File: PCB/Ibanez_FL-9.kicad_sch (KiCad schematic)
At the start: 131 parts, among them J1 INPUT, J2 OUTPUT, J3 EXT_DC, Q101 2SC2458GR, Q102 2SC2458GR, Q103 2SK44SPC, Q104 2SC2458GR, Q105 2SC2458GR, Q106 2SC2458GR, Q107 2SA1048Y/GR, Q108A 2SC1583F, Q108B 2SC1583F, Q109 2SC2458GR, U101 TL022, U102 TL022, U103 TL022, U104 MN3207, U105 MN3102, U106 LM2931-5.0_TO220

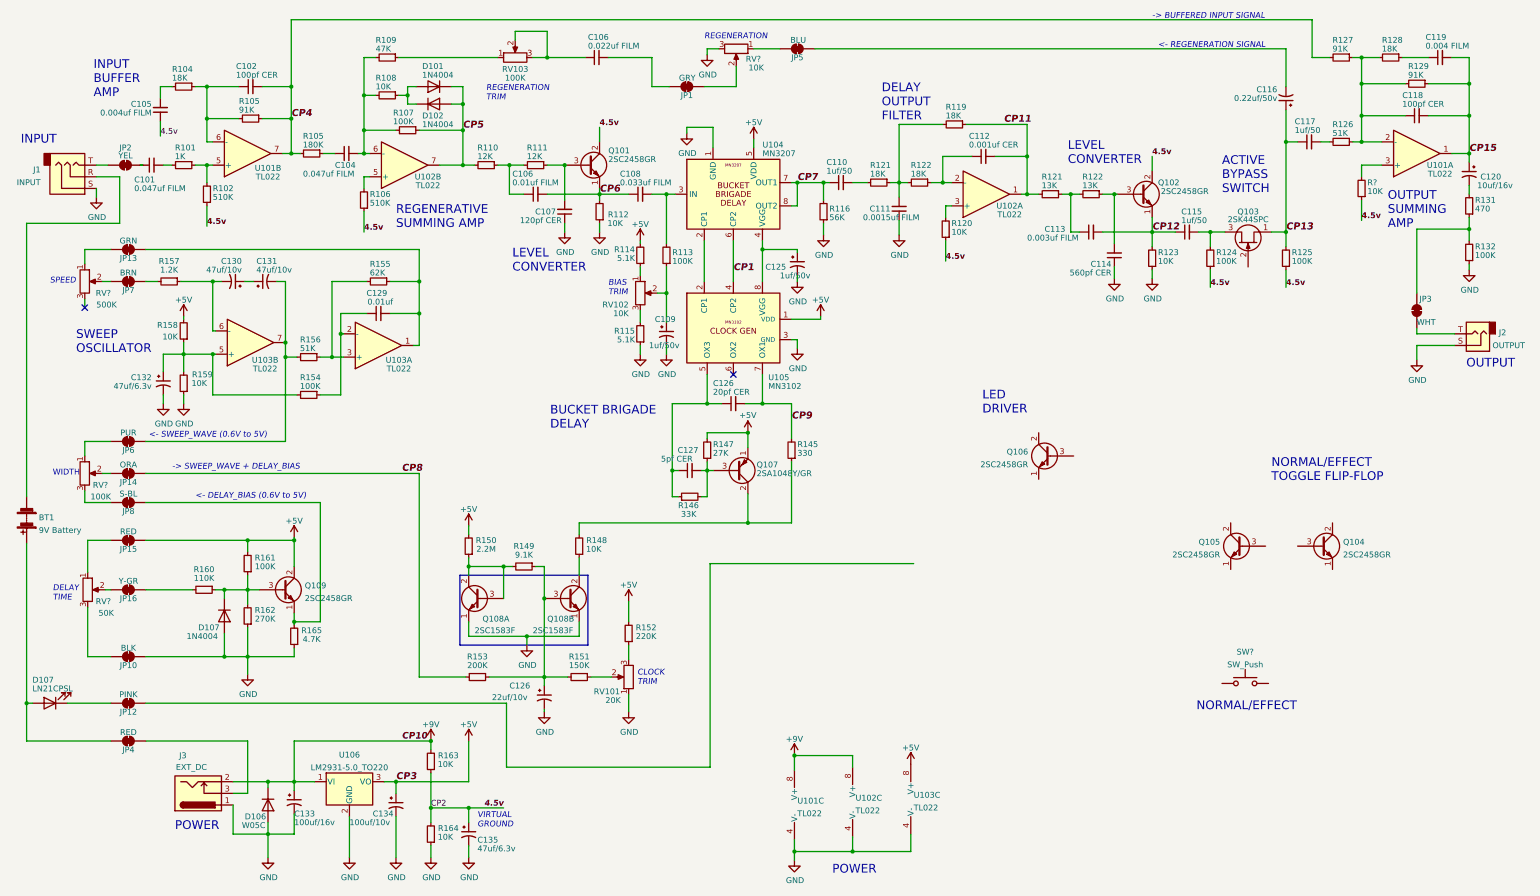
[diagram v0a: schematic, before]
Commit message: update docs; add BOM
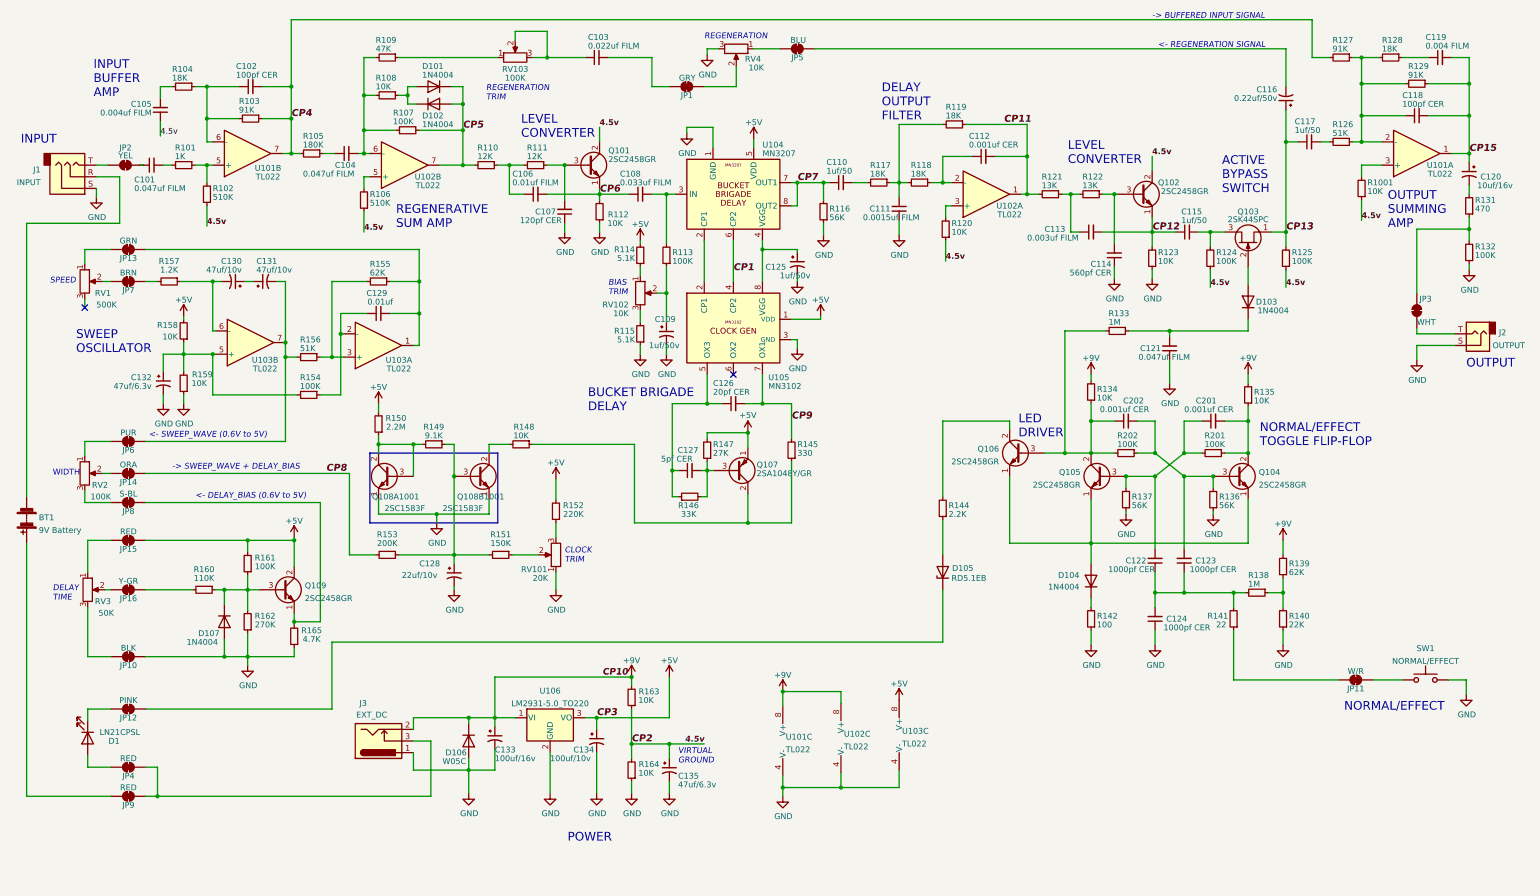
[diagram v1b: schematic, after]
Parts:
- added C121: 0.047uf FILM, Capacitor_SMD:C_0805_2012Metric, symbol Device:C_Small
- added C122, C123, C124: 1000pf CER, Capacitor_SMD:C_0805_2012Metric, symbol Device:C_Small
- added C201, C202: 0.001uf CER, Capacitor_SMD:C_0805_2012Metric, symbol Device:C_Small
- added D103, D104: 1N4004, Diode_THT:D_DO-35_SOD27_P7.62mm_Horizontal, symbol Diode:1N4448
- added D105: RD5.1EB, symbol Device:D_Zener
- added JP11: W/R, symbol Jumper:SolderJumper_2_Bridged
- added JP9: RED, symbol Jumper:SolderJumper_2_Bridged
- added R133, R138: 1M, Resistor_SMD:R_0805_2012Metric, symbol Device:R_Small
- added R134, R135: 10K, Resistor_SMD:R_0805_2012Metric, symbol Device:R_Small
- added R136, R137: 56K, Resistor_SMD:R_0805_2012Metric, symbol Device:R_Small
- added R139: 62K, Resistor_SMD:R_0805_2012Metric, symbol Device:R_Small
- added R140: 22K, Resistor_SMD:R_0805_2012Metric, symbol Device:R_Small
- added R141: 22, Resistor_SMD:R_0805_2012Metric, symbol Device:R_Small
- added R142: 100, Resistor_SMD:R_0805_2012Metric, symbol Device:R_Small
- added R144: 2.2K, Resistor_SMD:R_0805_2012Metric, symbol Device:R_Small
- added R201, R202: 100K, Resistor_SMD:R_0805_2012Metric, symbol Device:R_Small
- SW1: renamed from SW?; value SW_Push -> NORMAL/EFFECT
- gave numbers to parts that had none: 5
- renumbered C106 to C103, C126 to C128, D107 to D1, Q108A to Q108A1001, Q108B to Q108B1001, R105 to R103, R121 to R117, R122 to R118
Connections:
- net +9V: now also R134.2, R135.2, R139.2
- net GND: now also SW1.2, C121.1, C124.1, R136.1, R137.1, R140.1, R142.1
- net at D1.2 (A), JP4.1 (A): no longer BT1.1 (+)
- net at Q106.1 (E): now also Q104.1 (E), Q105.1 (E), D104.2 (A)
- net at Q106.2 (C): now also R144.2
- net at Q106.3 (B): now also Q105.2 (C), C202.1, R133.2, R134.1, R202.2
- net at Q108B1001.2 (C): now also R148.2; no longer R148.1
- net at JP12.2 (B): now also D105.1 (K)
- net at Q107.2 (C), R145.1: now also R148.1; no longer R148.2
- net at Q105.3 (B): now also C122.2, C201.1, R137.2, R201.2
- net at SW1.1: now also JP11.2 (B)
- net at Q104.2 (C): now also C201.2, R135.1, R201.1
- net at Q104.3 (B): now also C123.2, C202.2, R136.2, R202.1
- net at J3.3, JP4.2 (B): now also JP9.2 (B)
- net at Q103.2 (G): now also D103.2 (A)
- new net: D105.2 (A), R144.1
- new net: C122.1, C123.1, C124.2, R138.2, R141.2
- new net: JP11.1 (A), R141.1
- new net: C121.2, D103.1 (K), R133.1
- new net: BT1.1 (+), JP9.1 (A)
- new net: R138.1, R139.1, R140.2
- new net: D104.1 (K), R142.2
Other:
- note added: "REGENERATIVE SUM AMP"
- note removed: "REGENERATIVE SUMMING AMP"
- moved on the sheet: C128, C133, C134, C135, D1, D106, D107, J3, JP12, JP4, Q104, Q105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

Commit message: update docs; correct component labels and footprints
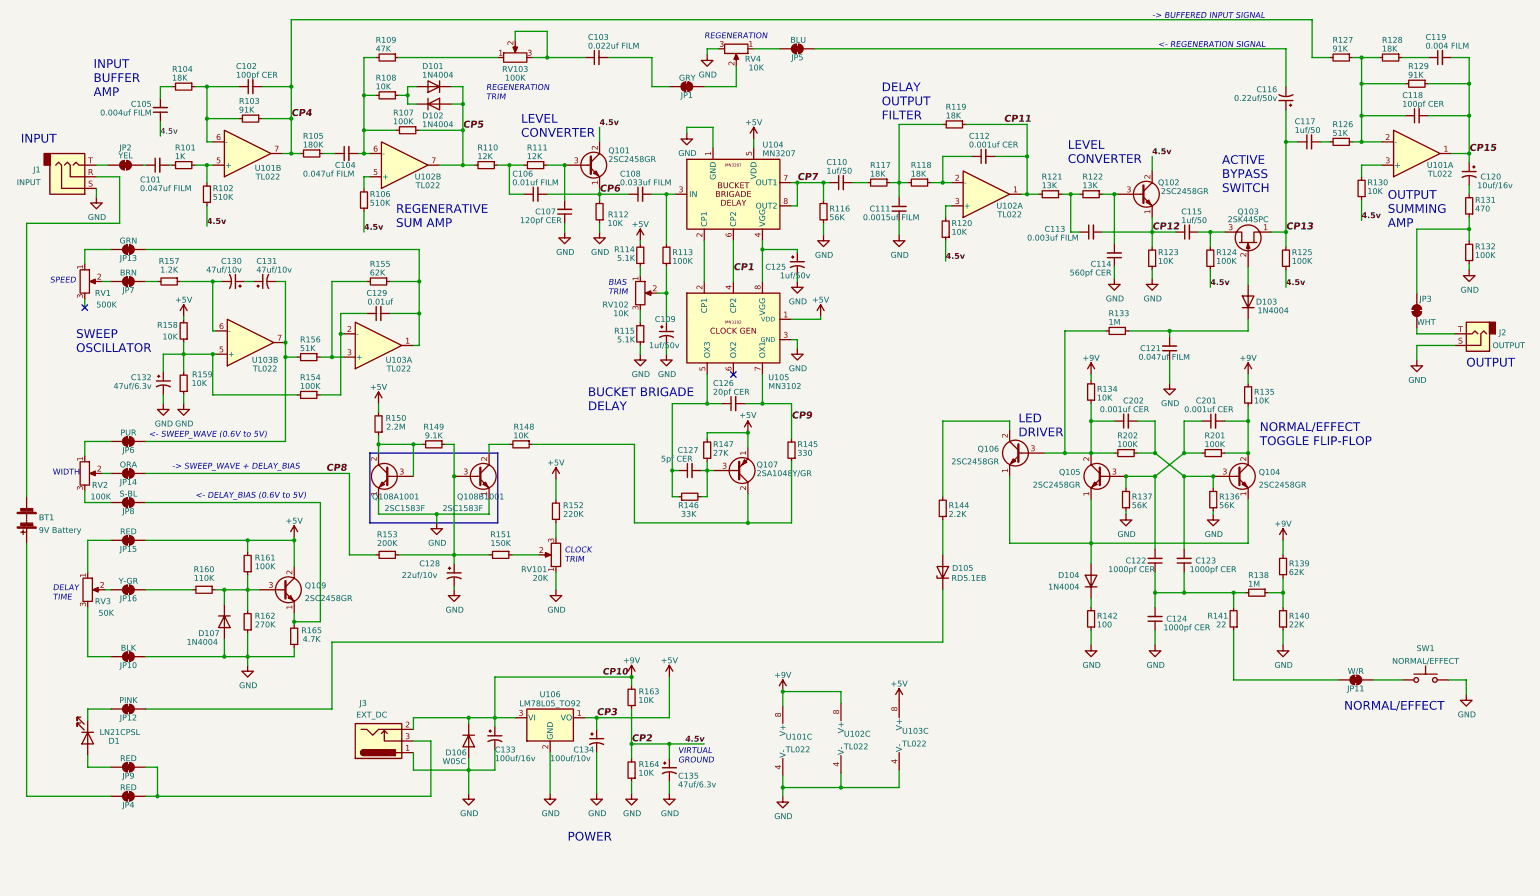
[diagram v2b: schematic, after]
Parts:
- removed U106: LM2931-5.0_TO220, Package_TO_SOT_THT:TO-220-3_Vertical, symbol Regulator_Linear:LM2931-5.0_TO220
- added U106: LM78L05_TO92, Package_TO_SOT_THT:TO-92_Inline, symbol Regulator_Linear:LM78L05_TO92
- BT1: footprint (none) -> Battery:BatteryHolder_MPD_BA9VPC_1xPP3
- C101, C103, C104, C105, C106, C108, C111, C113, C119, C121: footprint Capacitor_SMD:C_0805_2012Metric -> Capacitor_THT:C_Rect_L7.0mm_W2.5mm_P5.00mm
- C102, C107, C112, C114, C118, C122, C123, C124, C126, C127, C129, C201, C202: footprint Capacitor_SMD:C_0805_2012Metric -> Capacitor_THT:C_Disc_D3.0mm_W2.0mm_P2.50mm
- C109, C125: footprint Capacitor_SMD:CP_Elec_6.6x6.6 -> Capacitor_THT:CP_Radial_D4.0mm_P1.50mm
- C110, C115, C117: footprint Capacitor_SMD:C_0805_2012Metric -> Capacitor_THT:CP_Radial_D4.0mm_P1.50mm
- C116, C120, C128, C130, C131, C132, C135: footprint Capacitor_SMD:CP_Elec_6.6x6.6 -> Capacitor_THT:CP_Radial_D5.0mm_P2.50mm
- C133: footprint Capacitor_SMD:CP_Elec_6.6x6.6 -> Capacitor_THT:CP_Radial_D7.5mm_P2.50mm
- C134: footprint Capacitor_SMD:CP_Elec_6.6x6.6 -> Capacitor_THT:CP_Radial_D8.0mm_P3.80mm
- D1: footprint LED_SMD:LED_0805_2012Metric -> LED_THT:LED_D3.0mm_Clear
- D105: footprint (none) -> Diode_THT:D_DO-15_P2.54mm_Vertical_KathodeUp
- J3: footprint (none) -> Connector_BarrelJack:BarrelJack_Wuerth_6941xx301002
- JP1, JP10, JP11, JP12, JP13, JP14, JP15, JP16, JP2, JP3, JP4, JP5, JP6, JP7, JP8, JP9: footprint (none) -> Connector_Wire:SolderWire-0.5sqmm_1x01_D0.9mm_OD2.1mm
- Q103: footprint (none) -> Package_TO_SOT_THT:TO-92_Inline
- R101, R102, R103, R104, R105, R106, R107, R108, R109, R110, R111, R112, R113, R114, R115, R116, R117, R118, R119, R120, R121, R122, R123, R124, R125, R126, R127, R128, R129, R131, R132, R133, R134, R135, R136, R137, R138, R139, R140, R141, R142, R144, R145, R146, R147, R148, R149, R150, R151, R152, R153, R154, R155, R156, R157, R158, R159, R160, R161, R162, R163, R164, R165, R201, R202: footprint Resistor_SMD:R_0805_2012Metric -> Resistor_THT:R_Axial_DIN0204_L3.6mm_D1.6mm_P2.54mm_Vertical
- R130: renamed from R1001; footprint Resistor_SMD:R_0805_2012Metric -> Resistor_THT:R_Axial_DIN0204_L3.6mm_D1.6mm_P2.54mm_Vertical
- RV1, RV101, RV102, RV103, RV2, RV3, RV4: footprint (none) -> Potentiometer_THT:Potentiometer_ACP_CA6-H2,5_Horizontal
- SW1: footprint (none) -> Button_Switch_THT:SW_PUSH-12mm
- U101, U102, U103, U104, U105: footprint (none) -> Package_DIP:DIP-8_W7.62mm
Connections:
- net +5V: now also U106.1 (VO)
- net +9V: now also U106.3 (VI)
- net GND: now also U106.2 (GND)
- net at D1.2 (A): now also JP9.1 (A); no longer JP4.1 (A)
- net at BT1.1 (+): now also JP4.1 (A); no longer JP9.1 (A)
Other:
- moved on the sheet: C101, JP4, JP9

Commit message: update pcb layout
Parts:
- C101: footprint Capacitor_THT:C_Rect_L7.0mm_W2.5mm_P5.00mm -> Capacitor_THT:C_Rect_L7.2mm_W3.5mm_P5.00mm_FKS2_FKP2_MKS2_MKP2
- C104: footprint Capacitor_THT:C_Rect_L7.0mm_W2.5mm_P5.00mm -> Capacitor_THT:C_Rect_L7.0mm_W2.0mm_P5.00mm
- C133: footprint Capacitor_THT:CP_Radial_D7.5mm_P2.50mm -> Capacitor_THT:CP_Radial_D6.3mm_P2.50mm
- C134: footprint Capacitor_THT:CP_Radial_D8.0mm_P3.80mm -> Capacitor_THT:CP_Radial_D5.0mm_P2.00mm
- D101, D102: footprint Diode_THT:D_DO-35_SOD27_P7.62mm_Horizontal -> Diode_THT:D_T-1_P2.54mm_Vertical_KathodeUp
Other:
- note added: "as-built: 0.02uf FILM"
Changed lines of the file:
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@@
   (title_block
     (title "Ibanez_FL-9_Flanger_Pedal MP-FL0601")
-    (date "2022-11-21")
+    (date "2022-11-22")
     (rev "v01")
     (company "Cedar Grove Studios")
@@
     (effects (font (size 1.905 1.905)) (justify left bottom))
   )
+  (text "as-built:\n0.02uf FILM" (at 76.2 52.705 0)
+    (effects (font (size 1.27 1.27)) (justify left bottom))
+  )
   (text "CLOCK\nTRIM" (at 133.35 133.35 0)
     (effects (font (size 1.27 1.27) italic) (justify left bottom))
@@
       (effects (font (size 1.27 1.27)) (justify left))
     )
-    (property "Footprint" "Capacitor_THT:CP_Radial_D7.5mm_P2.50mm" (id 2) (at 118.11 171.45 0)
+    (property "Footprint" "Capacitor_THT:CP_Radial_D6.3mm_P2.50mm" (id 2) (at 118.11 171.45 0)
       (effects (font (size 1.27 1.27)) hide)
     )
@@
       (effects (font (size 1.27 1.27)) (justify left))
     )
-    (property "Footprint" "Capacitor_THT:CP_Radial_D8.0mm_P3.80mm" (id 2) (at 140.335 172.085 0)
+    (property "Footprint" "Capacitor_THT:CP_Radial_D5.0mm_P2.00mm" (id 2) (at 140.335 172.085 0)
       (effects (font (size 1.27 1.27)) hide)
     )
@@
       (effects (font (size 1.27 1.27)) (justify right))
     )
-    (property "Footprint" "Capacitor_THT:C_Rect_L7.0mm_W2.5mm_P5.00mm" (id 2) (at 85.725 43.815 0)
+    (property "Footprint" "Capacitor_THT:C_Rect_L7.0mm_W2.0mm_P5.00mm" (id 2) (at 85.725 43.815 0)
       (effects (font (size 1.27 1.27)) hide)
     )
@@
       (effects (font (size 1.27 1.27)) (justify right))
     )
-    (property "Footprint" "Capacitor_THT:C_Rect_L7.0mm_W2.5mm_P5.00mm" (id 2) (at 44.45 46.355 0)
+    (property "Footprint" "Capacitor_THT:C_Rect_L7.2mm_W3.5mm_P5.00mm_FKS2_FKP2_MKS2_MKP2" (id 2) (at 44.45 46.355 0)
       (effects (font (size 1.27 1.27)) hide)
     )
@@
       (effects (font (size 1.27 1.27)) (justify right))
     )
-    (property "Footprint" "Diode_THT:D_DO-35_SOD27_P7.62mm_Horizontal" (id 2) (at 104.775 24.765 0)
+    (property "Footprint" "Diode_THT:D_T-1_P2.54mm_Vertical_KathodeUp" (id 2) (at 104.775 24.765 0)
       (effects (font (size 1.27 1.27)) hide)
     )
@@
       (effects (font (size 1.27 1.27)) (justify left))
     )
-    (property "Footprint" "Diode_THT:D_DO-35_SOD27_P7.62mm_Horizontal" (id 2) (at 104.775 37.465 0)
+    (property "Footprint" "Diode_THT:D_T-1_P2.54mm_Vertical_KathodeUp" (id 2) (at 104.775 37.465 0)
       (effects (font (size 1.27 1.27)) hide)
     )
@@
     )
     (path "/c3c1cabe-2e9a-488d-8f40-6306f1a2336e"
-      (reference "C101") (unit 1) (value "0.047uf FILM") (footprint "Capacitor_THT:C_Rect_L7.0mm_W2.5mm_P5.00mm")
+      (reference "C101") (unit 1) (value "0.047uf FILM") (footprint "Capacitor_THT:C_Rect_L7.2mm_W3.5mm_P5.00mm_FKS2_FKP2_MKS2_MKP2")
     )
     (path "/695d5e86-cf8e-47d8-b5c0-e7d48f875f80"
@@
     )
     (path "/c346235f-4d02-486b-8c25-262da1e203e7"
-      (reference "C104") (unit 1) (value "0.047uf FILM") (footprint "Capacitor_THT:C_Rect_L7.0mm_W2.5mm_P5.00mm")
+      (reference "C104") (unit 1) (value "0.047uf FILM") (footprint "Capacitor_THT:C_Rect_L7.0mm_W2.0mm_P5.00mm")
     )
     (path "/077a8cee-b23f-4957-801a-aa35b59f1997"
@@
     )
     (path "/00000000-0000-0000-0000-0000611b49a7"
-      (reference "C133") (unit 1) (value "100uf/16v") (footprint "Capacitor_THT:CP_Radial_D7.5mm_P2.50mm")
+      (reference "C133") (unit 1) (value "100uf/16v") (footprint "Capacitor_THT:CP_Radial_D6.3mm_P2.50mm")
     )
     (path "/1e606b88-7641-4a41-9f6b-902ee963889f"
-      (reference "C134") (unit 1) (value "100uf/10v") (footprint "Capacitor_THT:CP_Radial_D8.0mm_P3.80mm")
+      (reference "C134") (unit 1) (value "100uf/10v") (footprint "Capacitor_THT:CP_Radial_D5.0mm_P2.00mm")
     )
     (path "/0f4a55bc-a8d2-4736-a9f5-016cffbfddbd"
@@
     )
     (path "/e8e17946-fe51-47d4-9523-932e0cd415cd"
-      (reference "D101") (unit 1) (value "1N4004") (footprint "Diode_THT:D_DO-35_SOD27_P7.62mm_Horizontal")
+      (reference "D101") (unit 1) (value "1N4004") (footprint "Diode_THT:D_T-1_P2.54mm_Vertical_KathodeUp")
     )
     (path "/ff0c2d69-4924-4851-9e12-f5f38ecf217b"
-      (reference "D102") (unit 1) (value "1N4004") (footprint "Diode_THT:D_DO-35_SOD27_P7.62mm_Horizontal")
+      (reference "D102") (unit 1) (value "1N4004") (footprint "Diode_THT:D_T-1_P2.54mm_Vertical_KathodeUp")
     )
     (path "/636f1130-2ada-4df5-a45d-16f01dff0ff5"

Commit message: update pcb layout
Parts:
- C108: footprint Capacitor_THT:C_Rect_L7.0mm_W2.5mm_P5.00mm -> Capacitor_THT:C_Rect_L7.0mm_W2.0mm_P5.00mm
- C128: value 22uf/10v -> 22uf/10v TAN; footprint Capacitor_THT:CP_Radial_D5.0mm_P2.50mm -> Capacitor_THT:CP_Radial_Tantal_D4.5mm_P5.00mm
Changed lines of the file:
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@@
       (effects (font (size 1.27 1.27)) (justify right))
     )
-    (property "Footprint" "Capacitor_THT:C_Rect_L7.0mm_W2.5mm_P5.00mm" (id 2) (at 149.86 52.705 0)
+    (property "Footprint" "Capacitor_THT:C_Rect_L7.0mm_W2.0mm_P5.00mm" (id 2) (at 149.86 52.705 0)
       (effects (font (size 1.27 1.27)) hide)
     )
@@
   (symbol (lib_id "Device:CP1_Small") (at 109.22 135.89 0) (unit 1)
     (in_bom yes) (on_board yes)
-    (property "Reference" "C128" (id 0) (at 101.6 133.35 0)
-      (effects (font (size 1.27 1.27)) (justify left))
-    )
-    (property "Value" "22uf/10v" (id 1) (at 97.79 135.89 0)
-      (effects (font (size 1.27 1.27)) (justify left))
-    )
-    (property "Footprint" "Capacitor_THT:CP_Radial_D5.0mm_P2.50mm" (id 2) (at 109.22 135.89 0)
+    (property "Reference" "C128" (id 0) (at 101.6 135.89 0)
+      (effects (font (size 1.27 1.27)) (justify left))
+    )
+    (property "Value" "22uf/10v TAN" (id 1) (at 99.695 137.795 0)
+      (effects (font (size 1.27 1.27)) (justify left))
+    )
+    (property "Footprint" "Capacitor_THT:CP_Radial_Tantal_D4.5mm_P5.00mm" (id 2) (at 109.22 135.89 0)
       (effects (font (size 1.27 1.27)) hide)
     )
@@
     )
     (path "/ba99d06d-930a-4fa1-a022-57872c1585a5"
-      (reference "C108") (unit 1) (value "0.033uf FILM") (footprint "Capacitor_THT:C_Rect_L7.0mm_W2.5mm_P5.00mm")
+      (reference "C108") (unit 1) (value "0.033uf FILM") (footprint "Capacitor_THT:C_Rect_L7.0mm_W2.0mm_P5.00mm")
     )
     (path "/ab885ec3-067d-48e4-8a08-ed3135c7cc40"
@@
     )
     (path "/d1d8c804-82a8-4d66-8de0-b275f8034f82"
-      (reference "C128") (unit 1) (value "22uf/10v") (footprint "Capacitor_THT:CP_Radial_D5.0mm_P2.50mm")
+      (reference "C128") (unit 1) (value "22uf/10v TAN") (footprint "Capacitor_THT:CP_Radial_Tantal_D4.5mm_P5.00mm")
     )
     (path "/00000000-0000-0000-0000-00005f94d28a"
